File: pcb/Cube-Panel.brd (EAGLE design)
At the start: 100 x 100 mm, 492 parts, among them IC1 MBI5041-GP, IC2 ATTINY(261/461/861)V-MAZ, Q1 DUAL_BJT_NPN_BIAS-PUMH2, X2 JP8ER

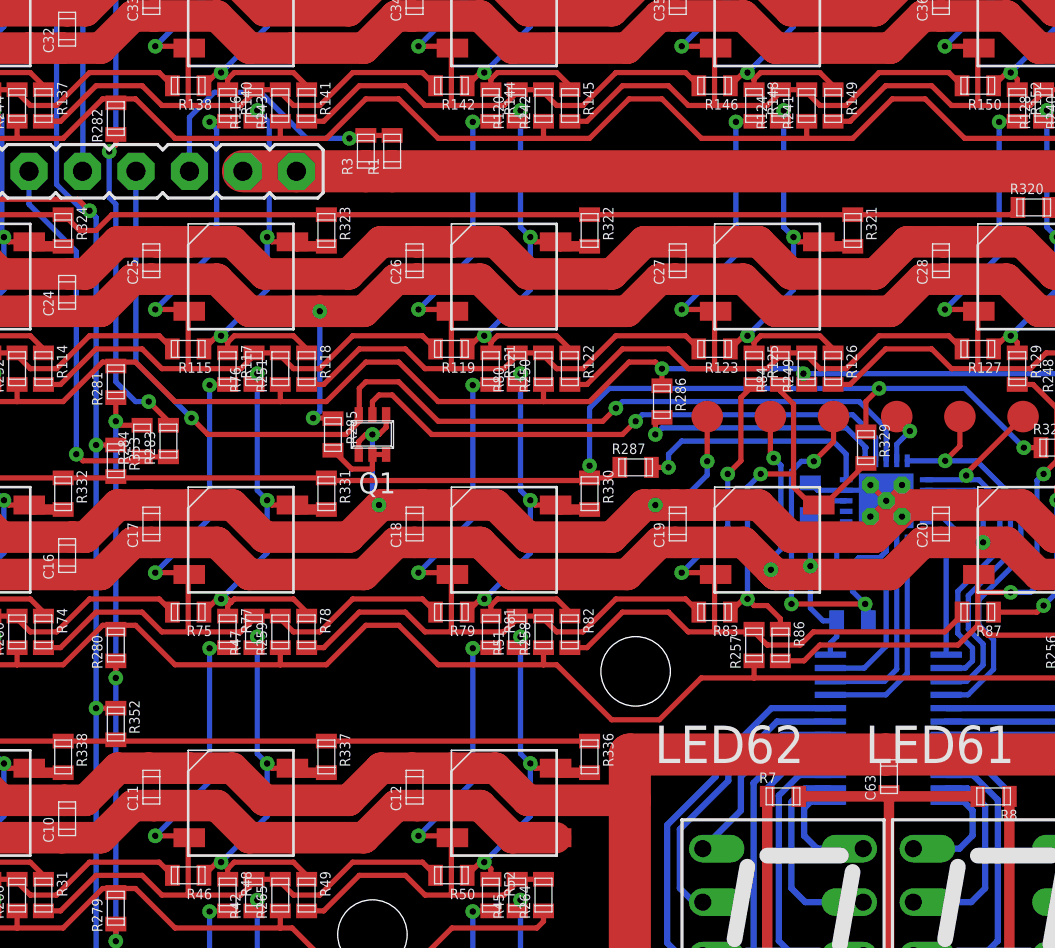
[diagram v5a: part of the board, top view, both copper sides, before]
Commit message: µC can now measure its own ID.
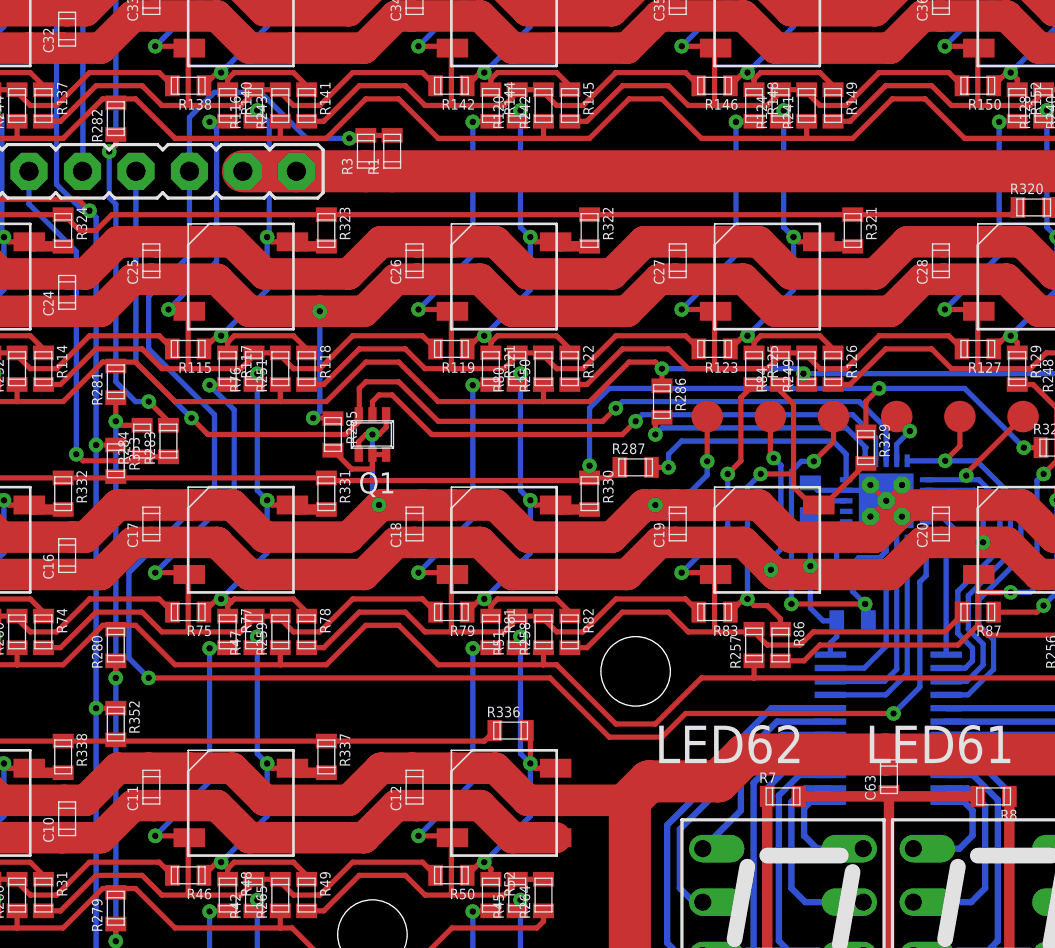
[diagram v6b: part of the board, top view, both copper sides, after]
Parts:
- moved R336 3.95 mm to (19.1, -27.8), turned to 0 degrees
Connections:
- removed net N$3: R1.P$2, R3.P$2, X2.6
- new net ID-SENSE: IC2.5, R1.P$2, R3.P$2, X2.6
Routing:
- net ID-SENSE: track 0.00 -> 88.6 mm, vias 0 -> 3
- net N$3: track 13.6 -> 0.00 mm, vias 1 -> 0
- net N$14: track 62.6 -> 58.3 mm
- net GND: track 982.9 -> 981.6 mm
- net IN17: track 36.6 -> 37.6 mm
- net IN25: track 36.9 -> 36.0 mm
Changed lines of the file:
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@@
 <setting verticaltext="up"/>
 </settings>
-<grid distance="0.325" unitdist="mm" unit="mm" style="lines" multiple="1" display="yes" altdistance="0.078125" altunitdist="mm" altunit="mm"/>
+<grid distance="0.3125" unitdist="mm" unit="mm" style="lines" multiple="1" display="yes" altdistance="0.078125" altunitdist="mm" altunit="mm"/>
 <layers>
 <layer number="1" name="Top" color="4" fill="1" visible="yes" active="yes"/>
@@
 <attribute name="PDP_NAME" value="Chipwiderstand, 0603, %VALUE%" x="-19.0625" y="139.0625" size="1" layer="27" font="vector" ratio="15" rot="R270" display="off"/>
 </element>
-<element name="R336" library="_Passive" package="0603" value="" x="22.8125" y="-29.0625" rot="R270">
-<attribute name="PDP_NAME" value="Chipwiderstand, 0603, %VALUE%" x="43.4375" y="132.5" size="1" layer="27" font="vector" ratio="15" rot="R270" display="off"/>
+<element name="R336" library="_Passive" package="0603" value="" x="19.0625" y="-27.8125">
+<attribute name="PDP_NAME" value="Chipwiderstand, 0603, %VALUE%" x="-142.5" y="-7.1875" size="1" layer="27" font="vector" ratio="15" display="off"/>
 </element>
 <element name="R337" library="_Passive" package="0603" value="" x="10.3125" y="-29.0625" rot="R270">
@@
 <wire x1="48.5" y1="-6.125" x2="48.5" y2="-18.75" width="2" layer="1"/>
 <wire x1="48.5" y1="-18.75" x2="48.5" y2="-28.95" width="2" layer="1"/>
-<wire x1="24.725" y1="-28.95" x2="36.875" y2="-28.95" width="2" layer="1"/>
 <wire x1="36.875" y1="-28.95" x2="48.5" y2="-28.95" width="2" layer="1"/>
-<wire x1="24.725" y1="-28.95" x2="24.725" y2="-31.125" width="2" layer="1"/>
 <contactref element="C1" pad="P$2"/>
 <contactref element="C2" pad="P$2"/>
@@
 <wire x1="12.5" y1="-13.75" x2="12.5" y2="-16.7875" width="0.25" layer="16"/>
 <wire x1="12.5" y1="-16.7875" x2="12.8125" y2="-17.1" width="0.25" layer="16"/>
+<wire x1="36.875" y1="-28.95" x2="30.2" y2="-28.95" width="2" layer="1"/>
+<wire x1="30.2" y1="-28.95" x2="28.925" y2="-30.225" width="2" layer="1"/>
+<wire x1="28.925" y1="-30.225" x2="25.625" y2="-30.225" width="2" layer="1"/>
+<wire x1="25.625" y1="-30.225" x2="24.725" y2="-31.125" width="2" layer="1"/>
 </signal>
 <signal name="VCC">
@@
 <wire x1="2.5" y1="-10.625" x2="3.75" y2="-10.625" width="0.25" layer="1"/>
 <wire x1="3.8" y1="-7.9" x2="3.7125" y2="-7.8125" width="0.25" layer="1"/>
-<wire x1="3.7125" y1="-7.8125" x2="2.1875" y2="-7.8125" width="0.25" layer="1"/>
-<via x="2.1875" y="-7.8125" extent="1-16" drill="0.3" shape="octagon"/>
+<wire x1="3.7125" y1="-7.8125" x2="2.8125" y2="-7.8125" width="0.25" layer="1"/>
+<via x="2.8125" y="-7.8125" extent="1-16" drill="0.3" shape="octagon"/>
 <via x="4.765625" y="1.09375" extent="1-16" drill="0.3" shape="octagon"/>
-<wire x1="5.1" y1="-4.9" x2="2.1875" y2="-7.8125" width="0.25" layer="16"/>
-<wire x1="5.1" y1="0.759375" x2="5.1" y2="-4.9" width="0.25" layer="16"/>
+<wire x1="5.1" y1="-5.525" x2="2.8125" y2="-7.8125" width="0.25" layer="16"/>
+<wire x1="5.1" y1="0.759375" x2="5.1" y2="-5.525" width="0.25" layer="16"/>
 <contactref element="R251" pad="P$2"/>
 <wire x1="10" y1="-10.625" x2="8.75" y2="-10.625" width="0.25" layer="1"/>
@@
 <wire x1="8.75" y1="-23.125" x2="8.125" y2="-22.5" width="0.25" layer="1"/>
 <wire x1="8.125" y1="-22.5" x2="8.125" y2="-22.375" width="0.25" layer="1"/>
-<wire x1="4.765625" y1="-11.40625" x2="4.765625" y2="-17.734375" width="0.25" layer="16"/>
-<wire x1="4.765625" y1="-17.734375" x2="2.1875" y2="-20.3125" width="0.25" layer="16"/>
+<wire x1="5.9375" y1="-16.5625" x2="2.1875" y2="-20.3125" width="0.25" layer="16"/>
 <wire x1="5.625" y1="-11.375" x2="4.796875" y2="-11.375" width="0.25" layer="1"/>
 <wire x1="4.796875" y1="-11.375" x2="4.765625" y2="-11.40625" width="0.25" layer="1"/>
+<wire x1="5.9375" y1="-16.5625" x2="5.9375" y2="-12.578125" width="0.25" layer="16"/>
+<wire x1="5.9375" y1="-12.578125" x2="4.765625" y2="-11.40625" width="0.25" layer="16"/>
 </signal>
 <signal name="OUT17">
@@
 <wire x1="19.375" y1="-23.515625" x2="19.53125" y2="-23.359375" width="0.25" layer="1"/>
 <contactref element="R336" pad="P$2"/>
-<wire x1="21.2" y1="-29.6" x2="21.4125" y2="-29.8125" width="0.5" layer="1"/>
-<wire x1="21.4125" y1="-29.8125" x2="22.8125" y2="-29.8125" width="0.5" layer="1"/>
+<wire x1="19.8125" y1="-27.8125" x2="20" y2="-28" width="0.25" layer="1"/>
+<wire x1="20" y1="-28" x2="20" y2="-29.375" width="0.25" layer="1"/>
 </signal>
 <signal name="OUT18">
@@
 <wire x1="-16.0875" y1="45.1875" x2="-14.6875" y2="45.1875" width="0.5" layer="1"/>
 </signal>
-<signal name="N$3">
-<contactref element="R1" pad="P$2"/>
-<contactref element="X2" pad="6"/>
-<contactref element="R3" pad="P$2"/>
-<wire x1="13.4375" y1="0.453125" x2="12.1875" y2="0.453125" width="0.25" layer="1"/>
-<via x="11.40625" y="0.3125" extent="1-16" drill="0.3" shape="octagon"/>
-<wire x1="11.40625" y1="0.3125" x2="11.546875" y2="0.453125" width="0.25" layer="1"/>
-<wire x1="11.546875" y1="0.453125" x2="12.1875" y2="0.453125" width="0.25" layer="1"/>
-<wire x1="3.81" y1="-1.25" x2="3.81" y2="1.31" width="0.25" layer="16"/>
-<wire x1="3.81" y1="1.31" x2="5" y2="2.5" width="0.25" layer="16"/>
-<wire x1="5" y1="2.5" x2="7.1875" y2="2.5" width="0.25" layer="16"/>
-<wire x1="7.1875" y1="2.5" x2="9.375" y2="0.3125" width="0.25" layer="16"/>
-<wire x1="9.375" y1="0.3125" x2="11.40625" y2="0.3125" width="0.25" layer="16"/>
-</signal>
 <signal name="SERIAL-BUS-TX">
 <contactref element="IC2" pad="17"/>
@@
 <wire x1="0.3125" y1="-23" x2="0.3125" y2="-22.8125" width="0.25" layer="1"/>
 <wire x1="-28.75" y1="-24.6875" x2="-29.375" y2="-24.6875" width="0.25" layer="1"/>
-<wire x1="28.1125" y1="-25.3125" x2="30.625" y2="-25.3125" width="0.25" layer="1"/>
+<wire x1="28.125" y1="-25.3125" x2="30.625" y2="-25.3125" width="0.25" layer="1"/>
 <wire x1="-28.75" y1="-24.6875" x2="-26.1375" y2="-27.3" width="0.25" layer="1"/>
 <wire x1="-26.1375" y1="-27.3" x2="-23.8625" y2="-27.3" width="0.25" layer="1"/>
 <wire x1="-21.25" y1="-24.6875" x2="-23.8625" y2="-27.3" width="0.25" layer="1"/>
-<wire x1="21.25" y1="-24.6875" x2="23.8625" y2="-27.3" width="0.25" layer="1"/>
-<wire x1="28.1125" y1="-25.3125" x2="26.125" y2="-27.3" width="0.25" layer="1"/>
-<wire x1="26.125" y1="-27.3" x2="23.8625" y2="-27.3" width="0.25" layer="1"/>
+<wire x1="21.25" y1="-24.6875" x2="24.0625" y2="-27.5" width="0.25" layer="1"/>
+<wire x1="28.125" y1="-25.3125" x2="25.9375" y2="-27.5" width="0.25" layer="1"/>
+<wire x1="25.9375" y1="-27.5" x2="24.0625" y2="-27.5" width="0.25" layer="1"/>
 </signal>
 <signal name="N$69">
@@
 <wire x1="-2.1875" y1="-28.3125" x2="0.3125" y2="-28.3125" width="0.25" layer="1"/>
 <wire x1="0.3125" y1="-28.3125" x2="10.3125" y2="-28.3125" width="0.25" layer="1"/>
-<wire x1="10.3125" y1="-28.3125" x2="22.8125" y2="-28.3125" width="0.25" layer="1"/>
 <wire x1="0.3125" y1="-28.25" x2="0.3125" y2="-28.3125" width="0.25" layer="1"/>
+<wire x1="18.3125" y1="-27.8125" x2="17.8125" y2="-28.3125" width="0.25" layer="1"/>
+<wire x1="17.8125" y1="-28.3125" x2="10.3125" y2="-28.3125" width="0.25" layer="1"/>
 </signal>
 <signal name="N$15">
@@
 <wire x1="27.1875" y1="-14.0625" x2="34.375" y2="-14.0625" width="0.25" layer="16"/>
 </signal>
+<signal name="ID-SENSE">
+<contactref element="IC2" pad="5"/>
+<contactref element="R1" pad="P$2"/>
+<contactref element="X2" pad="6"/>
+<contactref element="R3" pad="P$2"/>
+<wire x1="13.4375" y1="0.453125" x2="12.1875" y2="0.453125" width="0.25" layer="1"/>
+<via x="11.40625" y="0.3125" extent="1-16" drill="0.3" shape="octagon"/>
+<wire x1="11.40625" y1="0.3125" x2="11.546875" y2="0.453125" width="0.25" layer="1"/>
+<wire x1="11.546875" y1="0.453125" x2="12.1875" y2="0.453125" width="0.25" layer="1"/>
+<wire x1="3.81" y1="-1.25" x2="3.81" y2="1.31" width="0.25" layer="16"/>
+<wire x1="3.81" y1="1.31" x2="5" y2="2.5" width="0.25" layer="16"/>
+<wire x1="5" y1="2.5" x2="7.1875" y2="2.5" width="0.25" layer="16"/>
+<wire x1="7.1875" y1="2.5" x2="9.375" y2="0.3125" width="0.25" layer="16"/>
+<wire x1="9.375" y1="0.3125" x2="11.40625" y2="0.3125" width="0.25" layer="16"/>
+<wire x1="38.8" y1="-17.9" x2="38.8" y2="-20.45" width="0.25" layer="16"/>
+<wire x1="38.8" y1="-20.45" x2="38.5" y2="-20.75" width="0.25" layer="16"/>
+<wire x1="38.5" y1="-20.75" x2="38.5" y2="-25.75" width="0.25" layer="16"/>
+<wire x1="38.5" y1="-25.75" x2="37.25" y2="-27" width="0.25" layer="16"/>
+<via x="37.25" y="-27" extent="1-16" drill="0.3" shape="octagon"/>
+<wire x1="37.25" y1="-27" x2="27.375" y2="-27" width="0.25" layer="1"/>
+<wire x1="27.375" y1="-27" x2="26.25" y2="-28.125" width="0.25" layer="1"/>
+<wire x1="26.25" y1="-28.125" x2="23.75" y2="-28.125" width="0.25" layer="1"/>
+<wire x1="23.75" y1="-28.125" x2="20.9375" y2="-25.3125" width="0.25" layer="1"/>
+<wire x1="20.9375" y1="-25.3125" x2="1.875" y2="-25.3125" width="0.25" layer="1"/>
+<wire x1="5" y1="-12.8125" x2="5" y2="-16.25" width="0.25" layer="16"/>
+<wire x1="5" y1="-16.25" x2="0.9375" y2="-20.3125" width="0.25" layer="16"/>
+<wire x1="0.9375" y1="-20.3125" x2="0.9375" y2="-24.375" width="0.25" layer="16"/>
+<wire x1="0.9375" y1="-24.375" x2="1.875" y2="-25.3125" width="0.25" layer="16"/>
+<via x="1.875" y="-25.3125" extent="1-16" drill="0.3" shape="octagon"/>
+<wire x1="3.81" y1="-1.25" x2="3.81" y2="-5.2525" width="0.25" layer="16"/>
+<wire x1="3.81" y1="-5.2525" x2="1.875" y2="-7.1875" width="0.25" layer="16"/>
+<wire x1="1.875" y1="-7.1875" x2="1.875" y2="-9.6875" width="0.25" layer="16"/>
+<wire x1="1.875" y1="-9.6875" x2="5" y2="-12.8125" width="0.25" layer="16"/>
+</signal>
 </signals>
